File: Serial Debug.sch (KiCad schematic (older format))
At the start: 23 parts, among them J7 USB_OTG, U9 FT230XQ

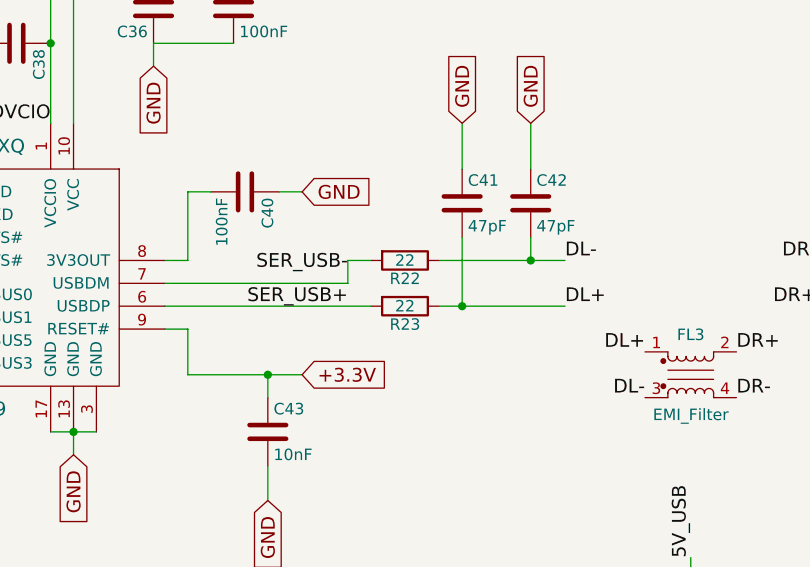
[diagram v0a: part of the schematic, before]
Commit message: This version contains the final revision before the part footprint verification.
- The fuse is now moved outside of the power module before any parts
- The wifi module has an additional pair of 22R differential resistors
- The minor moves in the power power supply of the wifi module
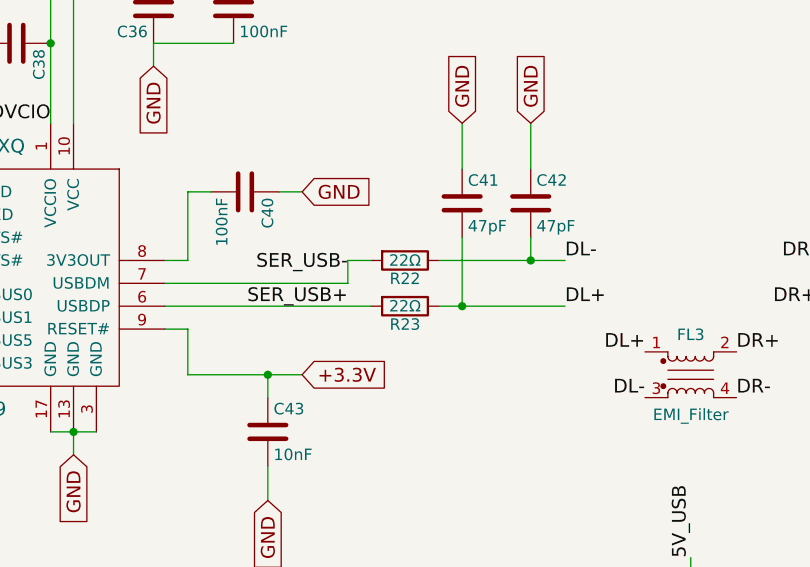
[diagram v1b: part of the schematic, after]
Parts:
- C44: orig (none) -> http://hu.farnell.com/multicomp/mcvvt6r3m101da1l/cap-alu-el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
- R22, R23: value 22 -> 22Ω
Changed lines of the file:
@@
 P 4150 3150
 F 0 "R22" V 4230 3150 50  0000 C CNN
-F 1 "22" V 4150 3150 50  0000 C CNN
+F 1 "22Ω" V 4150 3150 50  0000 C CNN
 F 2 "Resistors_SMD:R_0603_HandSoldering" V 4080 3150 50  0001 C CNN
 F 3 "http://hu.farnell.com/multicomp/mcwr06x22r0ftl/res-thick-film-22ohm-1-0-1w/dp/2447301" H 4150 3150 50  0001 C CNN
@@
 P 4150 3350
 F 0 "R23" V 4230 3350 50  0000 C CNN
-F 1 "22" V 4150 3350 50  0000 C CNN
+F 1 "22Ω" V 4150 3350 50  0000 C CNN
 F 2 "Resistors_SMD:R_0603_HandSoldering" V 4080 3350 50  0001 C CNN
 F 3 "http://hu.farnell.com/multicomp/mcwr06x22r0ftl/res-thick-film-22ohm-1-0-1w/dp/2447301" H 4150 3350 50  0001 C CNN
@@
 F 1 "100uF" H 5425 4750 50  0000 L CNN
 F 2 "Capacitors_SMD:CP_Elec_6.3x5.7" H 5438 4700 50  0001 C CNN
-F 3 "http://hu.farnell.com/multicomp/mcvvt6r3m101da1l/cap-alu-elec-100uf-6-3v-rad-can/dp/2611414" H 5400 4850 50  0001 C CNN
+F 3 "http://hu.farnell.com/multicomp/mcvvt6r3m101ea1l/cap-alu-elec-100uf-6-3v-rad-can/dp/2611415" H 5400 4850 50  0001 C CNN
+F 4 "http://hu.farnell.com/multicomp/mcvvt6r3m101da1l/cap-alu-elec-100uf-6-3v-rad-can/dp/2611414" H 5400 4850 60  0001 C CNN "orig"
 	1    5400 4850
 	1    0    0    -1

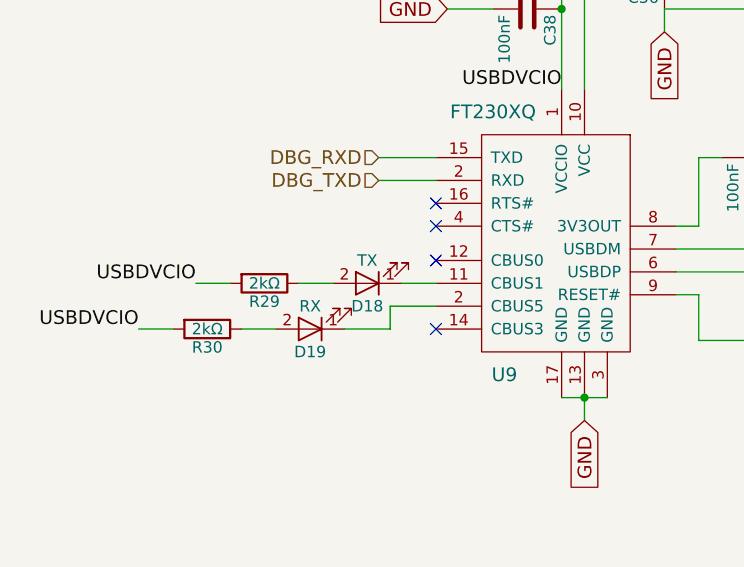
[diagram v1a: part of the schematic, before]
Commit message: new disposition of the parts
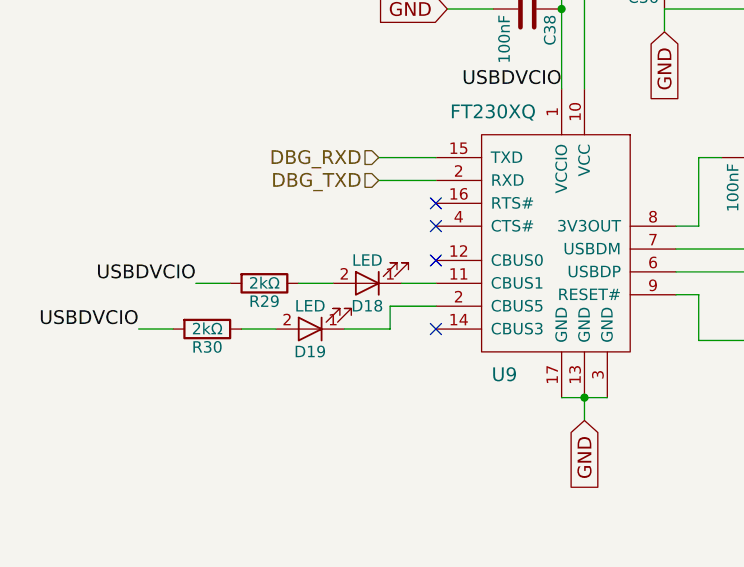
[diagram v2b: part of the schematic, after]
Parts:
- D18: value TX -> LED
- D19: value RX -> LED
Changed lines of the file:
@@
 	0    1    1    0
-$EndComp
-$Comp
-L LED D19
-U 1 1 59ADB2EA
-P 1500 3600
-F 0 "D19" H 1500 3700 50  0000 C CNN
-F 1 "RX" H 1500 3500 50  0000 C CNN
-F 2 "LEDs:LED_1206" H 1500 3600 50  0001 C CNN
-F 3 "http://hu.farnell.com/lumex/sml-lx1206gw-tr/led-2mm-x-1-6mm-green-10mcd-565nm/dp/2062262" H 1500 3600 50  0001 C CNN
-	1    1500 3600
-	-1   0    0    1
 $EndComp
 Wire Wire Line
@@
 	0    1    1    0
 $EndComp
-$Comp
-L LED D18
-U 1 1 59ADB916
-P 1750 3400
-F 0 "D18" H 1750 3500 50  0000 C CNN
-F 1 "TX" H 1750 3300 50  0000 C CNN
-F 2 "LEDs:LED_1206" H 1750 3400 50  0001 C CNN
-F 3 "http://hu.farnell.com/lumex/sml-lx1206gw-tr/led-2mm-x-1-6mm-green-10mcd-565nm/dp/2062262" H 1750 3400 50  0001 C CNN
-	1    1750 3400
-	-1   0    0    1
-$EndComp
 Wire Wire Line
 	1850 3600 1850 3500
@@
 Text Label 750  3600 2    60   ~ 0
 USBDVCIO
+$Comp
+L LED D19
+U 1 1 59B72417
+P 1500 3600
+F 0 "D19" H 1500 3700 50  0000 C CNN
+F 1 "LED" H 1500 3500 50  0000 C CNN
+F 2 "LEDs:LED_1206" H 1500 3600 50  0001 C CNN
+F 3 "http://hu.farnell.com/lumex/sml-lx15syc-tr/led-yellow-3mm-60mcd-590nm/dp/2062220" H 1500 3600 50  0001 C CNN
+	1    1500 3600
+	-1   0    0    1
+$EndComp
+$Comp
+L LED D18
+U 1 1 59B7256C
+P 1750 3400
+F 0 "D18" H 1750 3500 50  0000 C CNN
+F 1 "LED" H 1750 3300 50  0000 C CNN
+F 2 "LEDs:LED_1206" H 1750 3400 50  0001 C CNN
+F 3 "http://hu.farnell.com/lumex/sml-lx15syc-tr/led-yellow-3mm-60mcd-590nm/dp/2062220" H 1750 3400 50  0001 C CNN
+	1    1750 3400
+	-1   0    0    1
+$EndComp
 $EndSCHEMATC

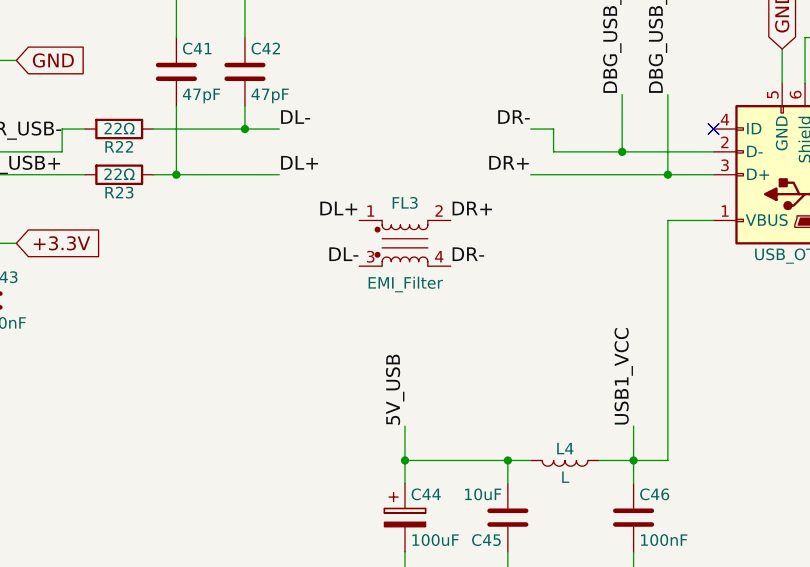
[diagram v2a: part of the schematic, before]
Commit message: I have re-routed the table after the footprints of the parts have been verified.
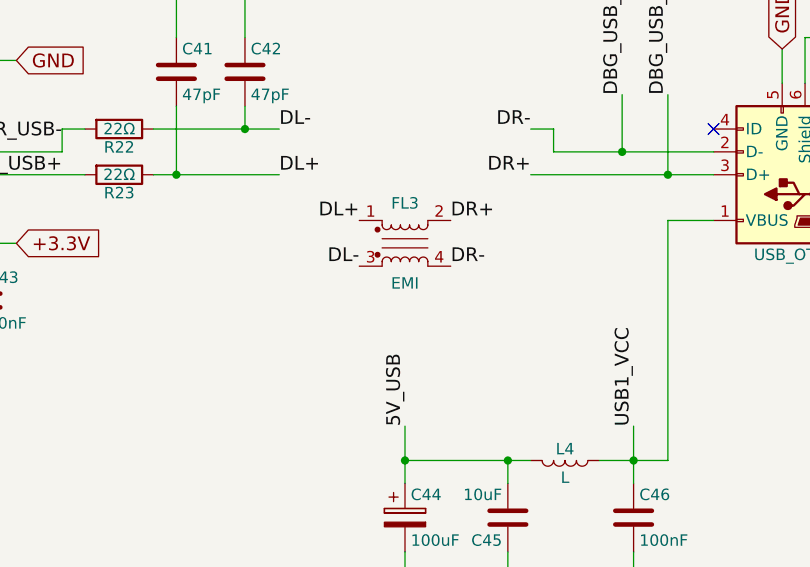
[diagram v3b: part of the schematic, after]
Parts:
- FL3: value EMI_Filter -> EMI
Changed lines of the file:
@@
 P 5400 3650
 F 0 "FL3" H 5400 3825 50  0000 C CNN
-F 1 "EMI_Filter" H 5400 3475 50  0000 C CNN
+F 1 "EMI" H 5400 3475 50  0000 C CNN
 F 2 "water:744233121" V 5400 3690 50  0001 C CNN
 F 3 "http://hu.farnell.com/wurth-elektronik/744233121/line-filter-lvds-0805-120ohm-0/dp/1848957" V 5400 3690 50  0001 C CNN
